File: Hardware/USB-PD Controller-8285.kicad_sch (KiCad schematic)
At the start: 27 parts, among them J1 Conn_01x07_Male, J10 Conn_Coaxial, J2 Conn_01x04_Male, J3 Conn_01x02_Male, J4 Conn_01x02_Male, J5 Conn_01x02_Male, J6 Conn_01x02_Male, J7 Conn_01x08_Male, J9 QWIIC_Stackable, Q1 UMH3N, U1 ESP8285H16, Y1 26.000MHz

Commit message: tweaks...
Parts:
- J7: LCSC (none) -> C2881786 + C2684732
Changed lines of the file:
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@@
+      (effects (font (size 1.27 1.27)) hide)
+    )
+    (property "LCSC" "C2881786 + C2684732" (id 4) (at 124.46 124.46 0)
       (effects (font (size 1.27 1.27)) hide)
     )

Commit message: messin' with the controller board
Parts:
- added J8: QWIIC, Connector_JST:JST_SH_BM04B-SRSS-TB_1x04-1MP_P1.00mm_Vertical, symbol Connector_QWIIC_Stackable:QWIIC_Stackable
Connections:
- net +3V3: now also J8.2 (Pin_2)
- net GND: now also J8.1 (Pin_1), J8.MP (MountPin)
- net SCL: now also J8.4 (Pin_4)
- net SDA: now also J8.3 (Pin_3)
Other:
- note added: "QWIIC"
- note added: "Stackable QWIIC"
- note removed: "I2C"
- moved on the sheet: J7, J9

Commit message: Expanding on the Controller Board functionality...
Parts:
- added SW1: SW_Push, Tinker:SW_Push_TS273014TP, symbol Switch:SW_Push
- J8: now left out of the parts list
- J9: now in the parts list
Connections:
- net GPIO is gone; now on net IO15: J7.8 (Pin_8)
- net IO14 is gone; now on net ATTACH: U1.9 (MTMS)
- net IO2 is gone; now on net ALERT: U1.14 (GPIO2)
- net IO5 is gone; now on net SCL: U1.24 (GPIO5)
- net POWER_OK2 is gone; now on net IO12: J7.4 (Pin_4)
- net POWER_OK3 is gone; now on net IO13: J7.6 (Pin_6)
- net RESET is gone; now on net IO16: J7.1 (Pin_1)
- net RST: now also SW1.1
- net SCL: no longer U1.21 (SD_CLK)
- net Vsec: now also SW1.2
- new net IO6: U1.21 (SD_CLK)

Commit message: ...
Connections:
- no-connect marks 7 -> 13
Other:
- moved on the sheet: J7

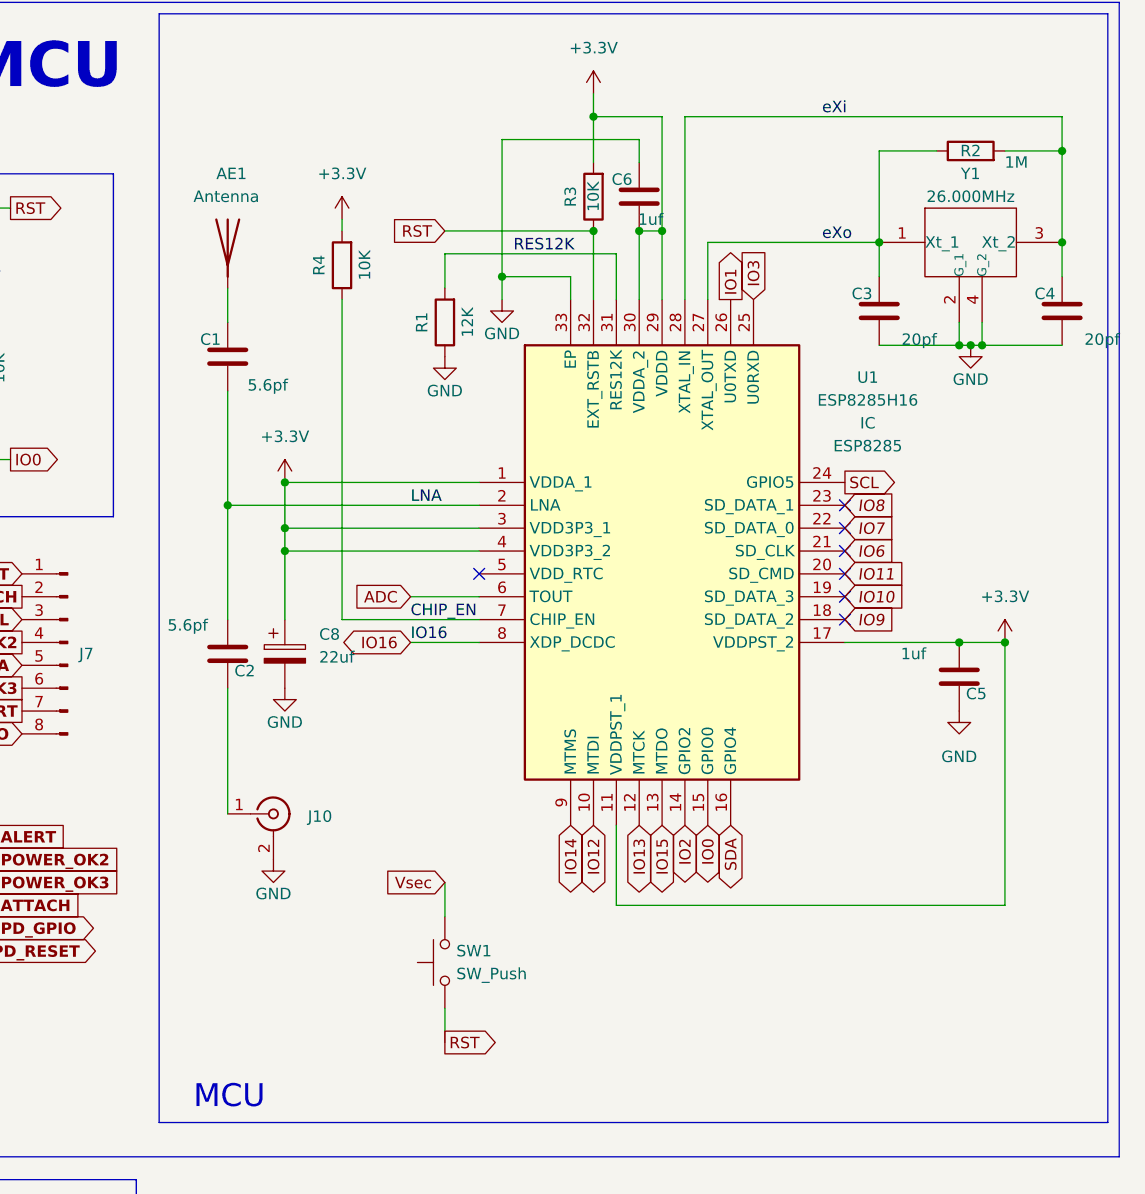
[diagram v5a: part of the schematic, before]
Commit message: Rabbit-Hole OCD... Redesigned Controller Board
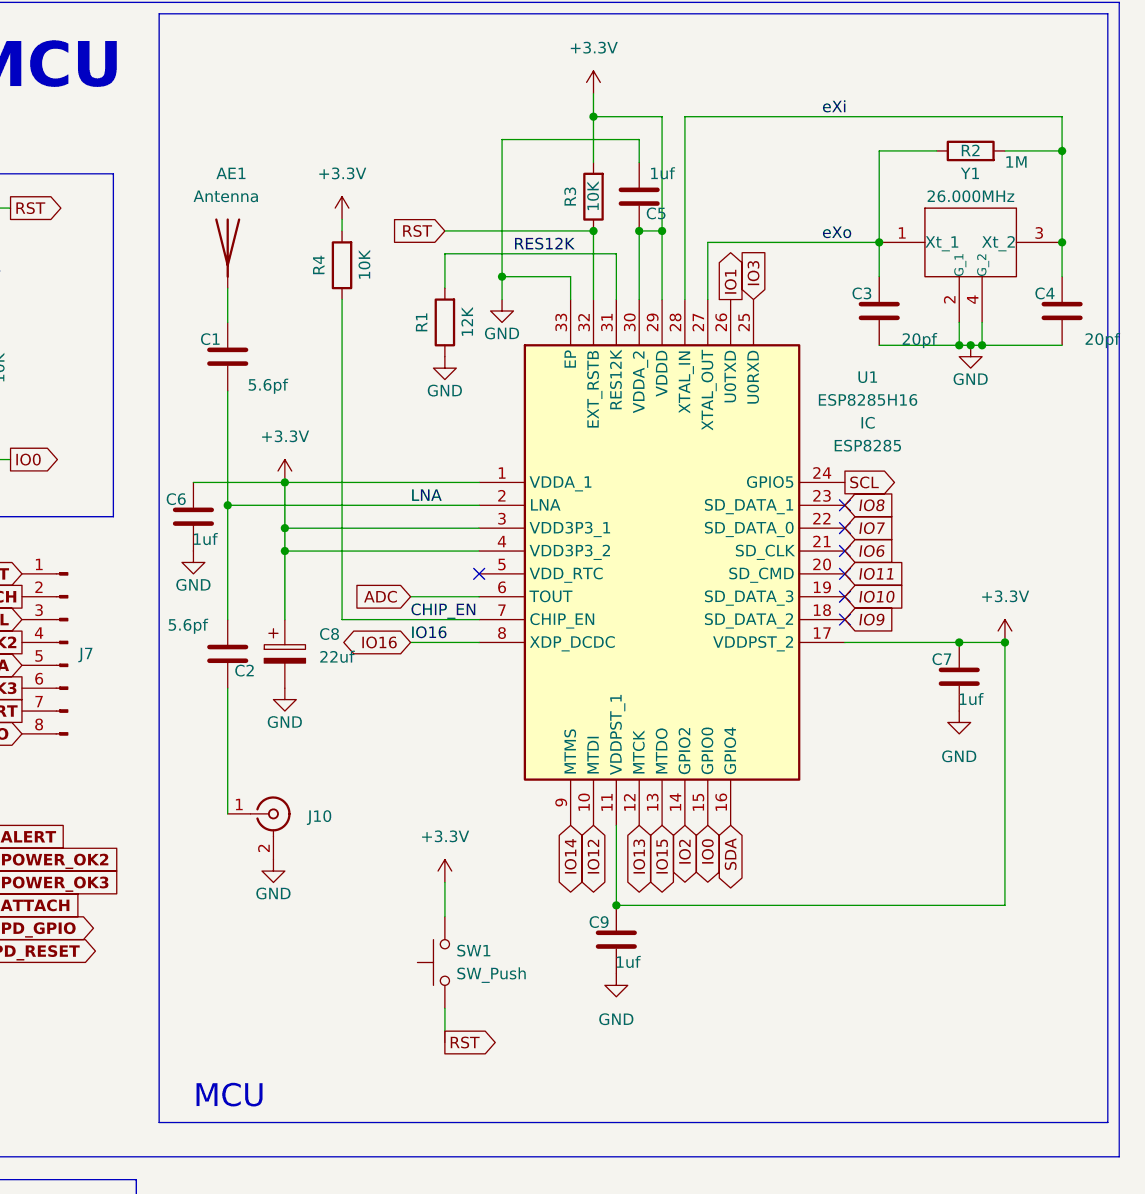
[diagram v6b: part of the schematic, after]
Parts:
- added C7, C9: 1uf, Capacitor_SMD:C_0603_1608Metric, symbol Device:C
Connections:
- net +3V3: now also C5.2, C6.2, SW1.2, C7.2, C9.2; no longer C5.1, C6.1
- net GND: now also C5.1, C6.1, C7.1, C9.1; no longer C5.2, C6.2
- net Vsec: no longer SW1.2
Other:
- moved on the sheet: C5, C6

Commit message: Much tweaking of Controller Board
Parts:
- removed J8: QWIIC, Connector_JST:JST_SH_BM04B-SRSS-TB_1x04-1MP_P1.00mm_Vertical, symbol Connector_QWIIC_Stackable:QWIIC_Stackable
- added J8: QWIIC_Vertical, Tinker:QWIIC_Vertical, symbol Connector_Generic_MountingPin:Conn_01x04_MountingPin
- J10: now in the parts list
- J9: footprint Tinker:QWIIC_Stackable -> Tinker:QWIIC_Stack_II; LCSC (none) -> C145956, C2881513, C2938401; Vendor LCSC C145956, -> (none)
- renumbered C8 to C1, C1 to C3, C3 to C4, C4 to C5, C5 to C6, C6 to C7, C7 to C8, R6 to R5, R7 to R6
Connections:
- net +3V3: now also J8.2 (Pin_2)
- net GND: now also J8.1 (Pin_1), J8.MP (MountPin)
- net SCL: now also J8.4 (Pin_4)
- net SDA: now also J8.3 (Pin_3)
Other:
- note added: "Vertical QWIIC"
- note removed: "QWIIC"

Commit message: Uber Rework!
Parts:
- J1: footprint Connector_PinHeader_2.54mm:PinHeader_1x07_P2.54mm_Vertical -> Tinker:Board_Stacker_7
- J2: footprint Tinker:PinHeader_1x04_P2.54mm_Vertical -> Tinker:Board_Stacker_4
- J3, J4, J5, J6: footprint Tinker:PinHeader_1x02_P2.54mm_Vertical -> Tinker:Board_Stacker_2
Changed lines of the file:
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@@
   (title_block
     (title "USB-C PD Controller")
-    (rev "0.0.3")
+    (rev "0.1.3")
     (company "The Nerd Mage")
     (comment 2 "Massively a WIP!")
@@
     (property "Reference" "J3" (id 0) (at 31.115 97.79 0))
     (property "Value" "Conn_01x02_Male" (id 1) (at 31.115 100.33 0))
-    (property "Footprint" "Tinker:PinHeader_1x02_P2.54mm_Vertical" (id 2) (at 31.75 102.87 0)
+    (property "Footprint" "Tinker:Board_Stacker_2" (id 2) (at 31.75 102.87 0)
       (effects (font (size 1.27 1.27)) hide)
     )
@@
       (effects (font (size 1.27 1.27)) (justify right))
     )
-    (property "Footprint" "Tinker:PinHeader_1x02_P2.54mm_Vertical" (id 2) (at 57.15 148.59 0)
+    (property "Footprint" "Tinker:Board_Stacker_2" (id 2) (at 57.15 148.59 0)
       (effects (font (size 1.27 1.27)) hide)
     )
@@
       (effects (font (size 1.27 1.27)) (justify right))
     )
-    (property "Footprint" "Tinker:PinHeader_1x04_P2.54mm_Vertical" (id 2) (at 31.75 34.29 0)
+    (property "Footprint" "Tinker:Board_Stacker_4" (id 2) (at 31.75 34.29 0)
       (effects (font (size 1.27 1.27)) hide)
     )
@@
     (property "Reference" "J4" (id 0) (at 55.245 97.79 0))
     (property "Value" "Conn_01x02_Male" (id 1) (at 55.245 100.33 0))
-    (property "Footprint" "Tinker:PinHeader_1x02_P2.54mm_Vertical" (id 2) (at 55.88 102.87 0)
+    (property "Footprint" "Tinker:Board_Stacker_2" (id 2) (at 55.88 102.87 0)
       (effects (font (size 1.27 1.27)) hide)
     )
@@
     (property "Reference" "J5" (id 0) (at 31.115 143.51 0))
     (property "Value" "Conn_01x02_Male" (id 1) (at 31.115 146.05 0))
-    (property "Footprint" "Tinker:PinHeader_1x02_P2.54mm_Vertical" (id 2) (at 31.75 148.59 0)
+    (property "Footprint" "Tinker:Board_Stacker_2" (id 2) (at 31.75 148.59 0)
       (effects (font (size 1.27 1.27)) hide)
     )
@@
       (effects (font (size 1.27 1.27)) hide)
     )
-    (property "Footprint" "Connector_PinHeader_2.54mm:PinHeader_1x07_P2.54mm_Vertical" (id 2) (at 102.87 50.8 0)
+    (property "Footprint" "Tinker:Board_Stacker_7" (id 2) (at 102.87 50.8 0)
       (effects (font (size 1.27 1.27)) hide)
     )
@@
     )
     (path "/ff08f666-d31b-45a5-8777-a0482d9fced1"
-      (reference "J1") (unit 1) (value "Conn_01x07_Male") (footprint "Connector_PinHeader_2.54mm:PinHeader_1x07_P2.54mm_Vertical")
+      (reference "J1") (unit 1) (value "Conn_01x07_Male") (footprint "Tinker:Board_Stacker_7")
     )
     (path "/ce562b82-4d15-4512-9ef8-80a89b06889d"
-      (reference "J2") (unit 1) (value "Conn_01x04_Male") (footprint "Tinker:PinHeader_1x04_P2.54mm_Vertical")
+      (reference "J2") (unit 1) (value "Conn_01x04_Male") (footprint "Tinker:Board_Stacker_4")
     )
     (path "/31399746-8e56-4d74-b787-07c634e0c687"
-      (reference "J3") (unit 1) (value "Conn_01x02_Male") (footprint "Tinker:PinHeader_1x02_P2.54mm_Vertical")
+      (reference "J3") (unit 1) (value "Conn_01x02_Male") (footprint "Tinker:Board_Stacker_2")
     )
     (path "/e516ae01-774d-4d4f-b0c4-6f2304b851fc"
-      (reference "J4") (unit 1) (value "Conn_01x02_Male") (footprint "Tinker:PinHeader_1x02_P2.54mm_Vertical")
+      (reference "J4") (unit 1) (value "Conn_01x02_Male") (footprint "Tinker:Board_Stacker_2")
     )
     (path "/fb3406f1-7439-4c3c-b07d-423418b2c3c6"
-      (reference "J5") (unit 1) (value "Conn_01x02_Male") (footprint "Tinker:PinHeader_1x02_P2.54mm_Vertical")
+      (reference "J5") (unit 1) (value "Conn_01x02_Male") (footprint "Tinker:Board_Stacker_2")
     )
     (path "/c84ab28b-75dd-4180-9570-ba047f49794b"
-      (reference "J6") (unit 1) (value "Conn_01x02_Male") (footprint "Tinker:PinHeader_1x02_P2.54mm_Vertical")
+      (reference "J6") (unit 1) (value "Conn_01x02_Male") (footprint "Tinker:Board_Stacker_2")
     )
     (path "/52b865ad-eda4-4c7d-8632-e0e9bcc50e71"
